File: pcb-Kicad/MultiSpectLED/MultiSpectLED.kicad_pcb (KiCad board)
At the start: 2 copper layers, 113.4 x 56 mm, 117 parts, among them J1 Conn_01x02_Female, J2 USB_C_Receptacle_USB2.0, SW1 NKK_HEXADEC, SW2 NKK_HEXADEC, U1 PAM2804, U10 PAM2804, U11 PAM2804, U12 PAM2804, U13 PAM2804, U14 PAM2804, U15 PAM2804, U16 PAM2804, U2 TeensyLC, U3 PAM2804, U4 PAM2804, U5 PAM2804, U6 PAM2804, U7 PAM2804, U8 PAM2804, U9 PAM2804

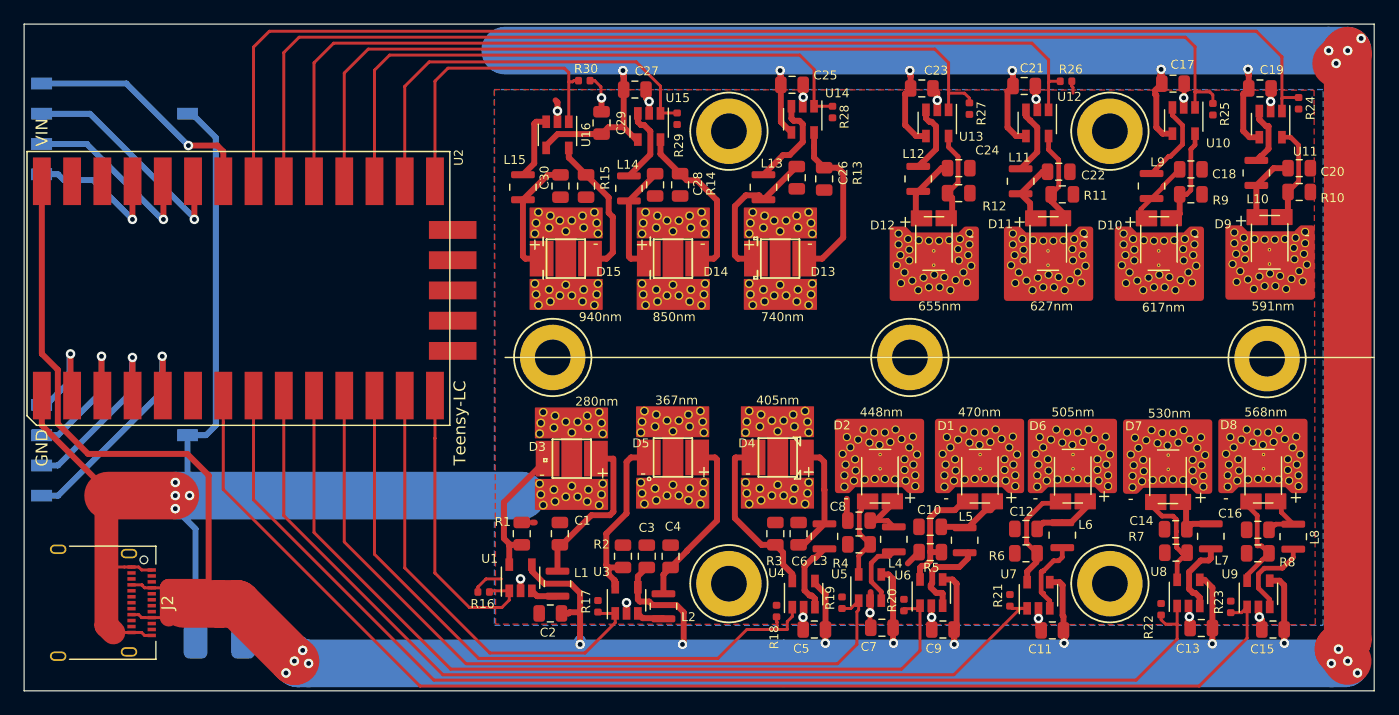
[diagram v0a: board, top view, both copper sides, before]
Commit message: Use boost driver for 280nm LED
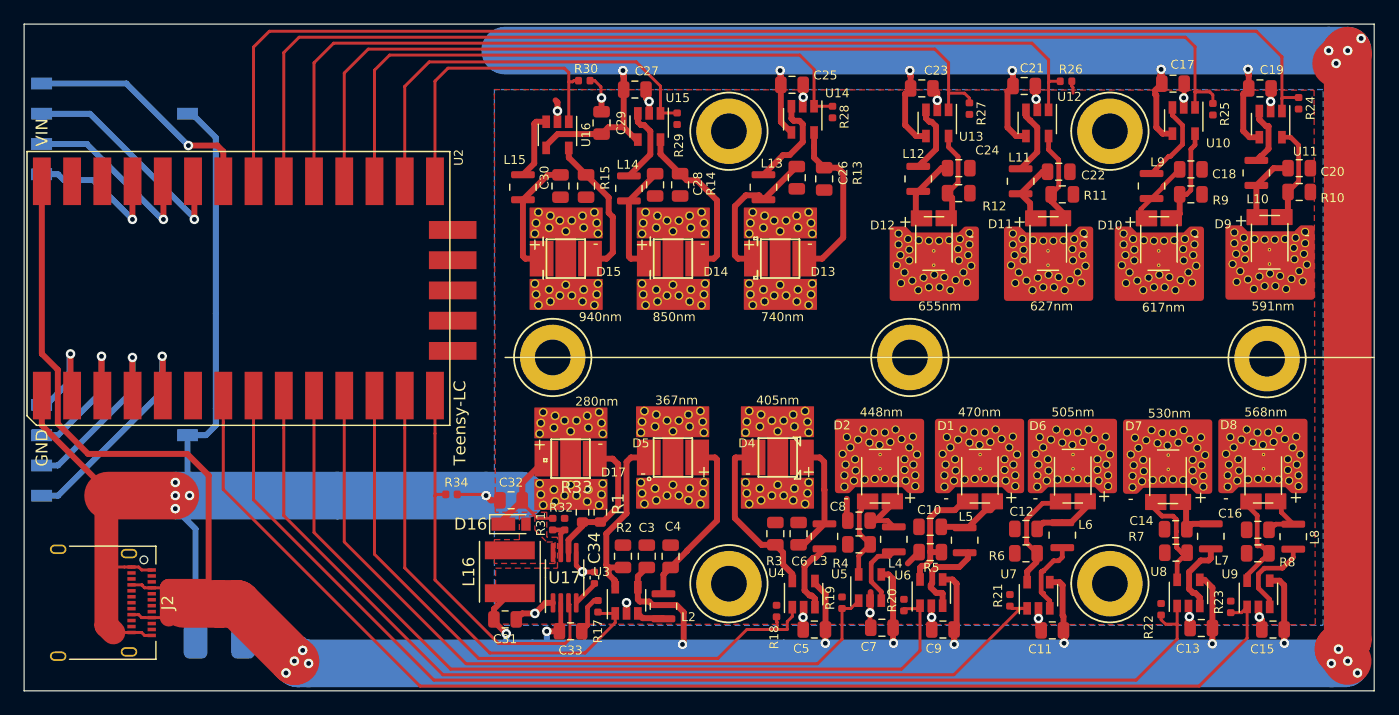
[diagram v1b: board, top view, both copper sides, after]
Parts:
- removed C1, C2: C, MultiSpectLED:C_0805_2012Metric
- removed D3: 280nm, MultiSpectLED:Luminus_XBT3535
- removed L1: 4.7u, MultiSpectLED:L_1007_2518Metric
- removed R16: 100K, MultiSpectLED:R_0402_1005Metric
- removed U1: PAM2804, MultiSpectLED:SOT-23-5
- added C31: 10u, MultiSpectLED:C_0805_2012Metric, F.Cu at (164.0, 115.0)
- added C32: 1u, MultiSpectLED:C_0805_2012Metric, F.Cu at (164.5, 105.0)
- added C33: 1u, MultiSpectLED:C_0805_2012Metric, F.Cu at (169.5, 116.0)
- added C34: 100n, Capacitor_SMD:C_0402_1005Metric, F.Cu at (171.5, 111.5)
- added D16: D_Schottky, Diode_SMD:D_TUMD2, F.Cu at (164.5, 107.0)
- added D17: 280nm, MultiSpectLED:Luminus_XBT3535, F.Cu at (169.5, 101.5)
- added L16: 22u, Inductor_SMD:L_Taiyo-Yuden_NR-50xx, F.Cu at (164.4, 111.0)
- added R31: 9.1k, MultiSpectLED:R_0402_1005Metric, F.Cu at (168.0, 107.0)
- added R32: 1.2k, MultiSpectLED:R_0402_1005Metric, F.Cu at (169.0, 107.0)
- added R33: .5, Resistor_SMD:R_0603_1608Metric, F.Cu at (170.5, 106.0)
- added R34: 100K, MultiSpectLED:R_0402_1005Metric, F.Cu at (159.5, 104.5)
- added U17: PAM2841, Package_SO:MSOP-8_3x3mm_P0.65mm, F.Cu at (169.0, 111.5)
- R1: value 0.2 -> .5; footprint MultiSpectLED:R_0805_2012Metric -> Resistor_SMD:R_0603_1608Metric
- moved R1 6.84 mm to (172.0, 106.0)
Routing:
- net Net-(C1-Pad1): track 13.9 -> 0.00 mm
- net Net-(C32-Pad1): track 0.00 -> 10.3 mm
- net /GND: track 148.0 -> 157.8 mm, vias 20 -> 22
- net /PWM_D3_280nm: track 25.1 -> 33.2 mm
- net Net-(R31-Pad2): track 0.00 -> 3.04 mm
- net /+5V: track 395.2 -> 397.9 mm, vias 26 -> 27
- net Net-(L1-Pad1): track 2.34 -> 0.00 mm
- net Net-(C34-Pad1): track 0.00 -> 2.26 mm
- net /PWM_D2_448nm: track 65.7 -> 63.5 mm
- net Net-(D17-Pad1): track 11.6 -> 12.3 mm
- added copper zone on F.Cu, net Net-(D16-Pad2)
